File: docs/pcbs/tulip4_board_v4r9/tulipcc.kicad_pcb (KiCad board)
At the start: 2 copper layers, 134 x 88 mm, 103 parts, among them J1 XF2M-4015-1A, J2 1734709-4, J3 217179-0001, J4 SJ2-35863B1, J5 217179-0001, J6 SJ2-35863B1, J7 SJ2-35863B1, J8 1734827-2, Q1 DMP3099L, SW1 JS102011JAQN, U1 ESP32-S3-WROOM-2-N32R8V, U10 MCP73832, U11 MAX17048G, U12 TPS7A4533DCQR, U13 MIC2875-5.0YMT, U2 MBT3904DW1T1G, U3 USBLC6-2SC6, U4 FT231XS, U5 MIC2005A-2YM5-TR, U6 H11L1SR2M, U7 USBLC6-2SC6, U8 PCM5101A-Q1, U9 TPA6110A2DGN

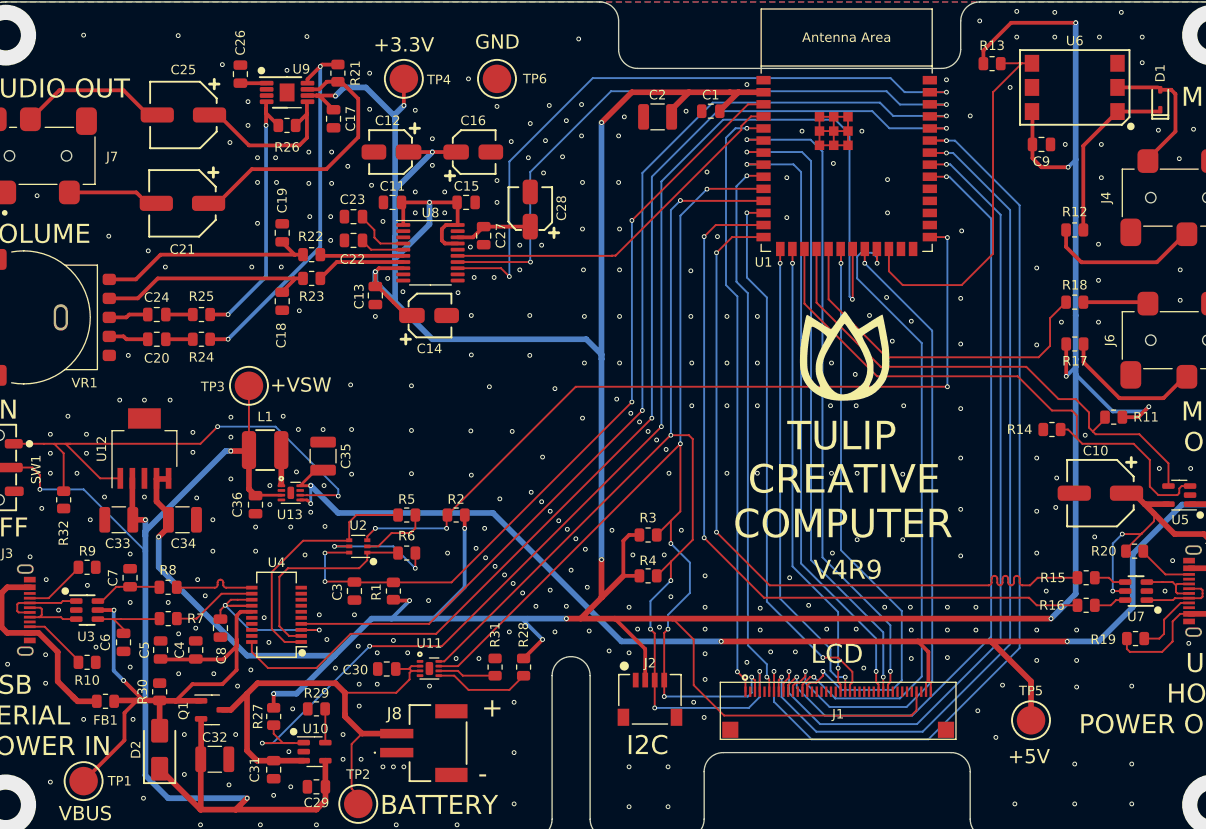
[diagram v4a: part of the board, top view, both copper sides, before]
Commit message: V4R9A: USB, Audio circuit fix. Updated component part #s.
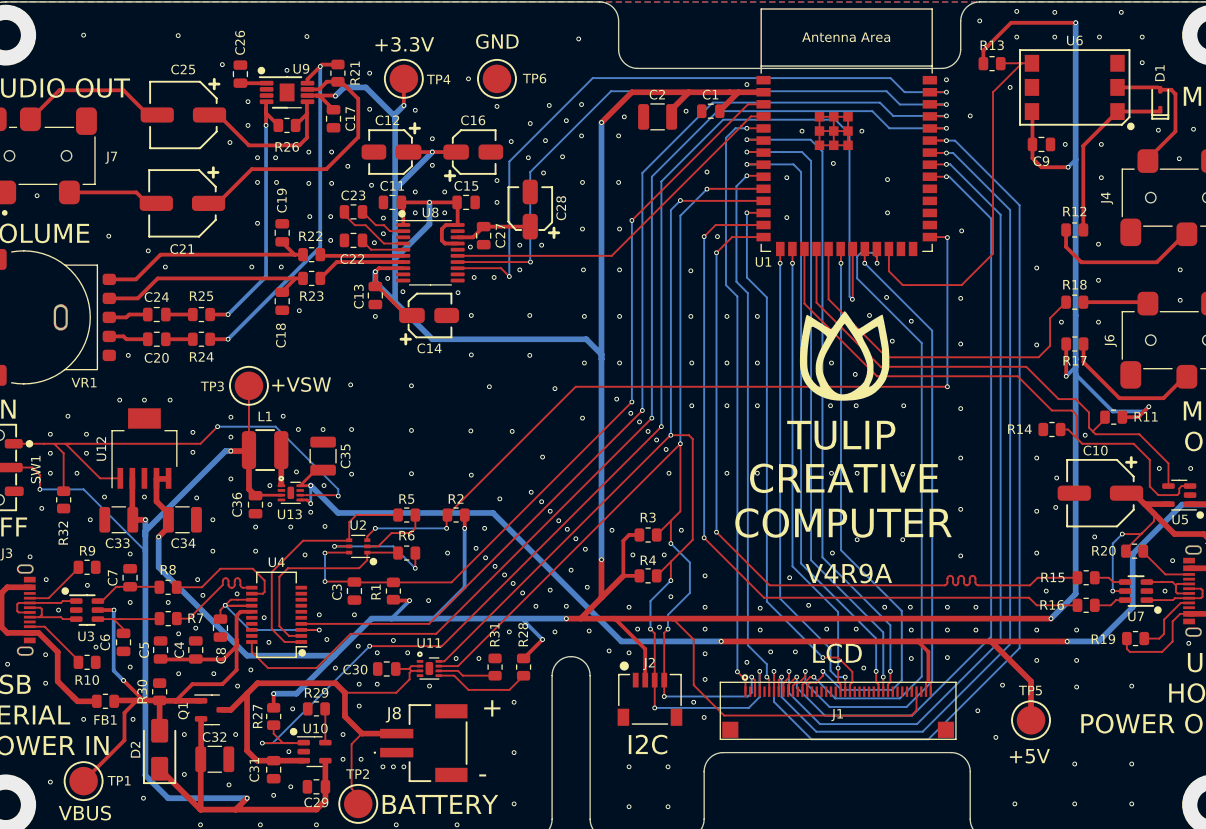
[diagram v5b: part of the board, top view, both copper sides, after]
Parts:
- U8: footprint Package_SO:TSSOP-20_4.4x6.5mm_P0.65mm -> tulipcc_footprint_lib:TSSOP-20_4.4x6.5mm_P0.65mm
- moved C23 0.50 mm to (40.1, -65.9), turned to 0 degrees
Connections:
- C23 pad 2: GND -> Net-(U8-CAPP)
- R7 pad 2: Net-(U4-USBDM) -> Net-(U4-USBDP)
- R8 pad 2: Net-(U4-USBDP) -> Net-(U4-USBDM)
- U8 pad 2: GND -> Net-(U8-CAPP)
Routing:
- net Net-(U8-CAPP): track 0.00 -> 5.13 mm
- net Net-(U4-USBDM): track 8.97 -> 13.2 mm
- net Net-(U4-USBDP): track 9.04 -> 12.1 mm
- net Net-(U8-CAPM): track 6.01 -> 7.74 mm
- net GND: vias 368 -> 371
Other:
- board text added: "V4R9A"
- board text removed: "V4R9"
